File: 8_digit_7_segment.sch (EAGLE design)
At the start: 9 parts, among them IC1 MAX7219CNG

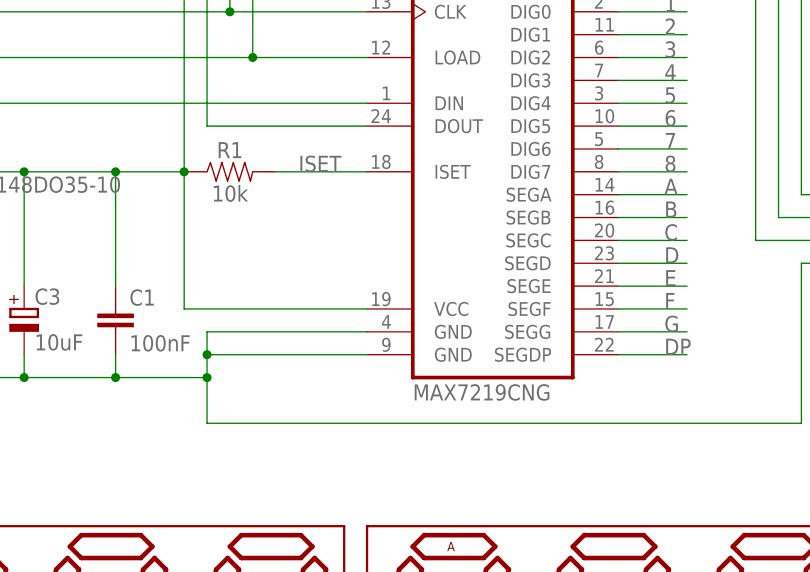
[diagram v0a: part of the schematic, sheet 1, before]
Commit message: Minor modifications, 3D components added to the Eagle files and new images added of the 3D model
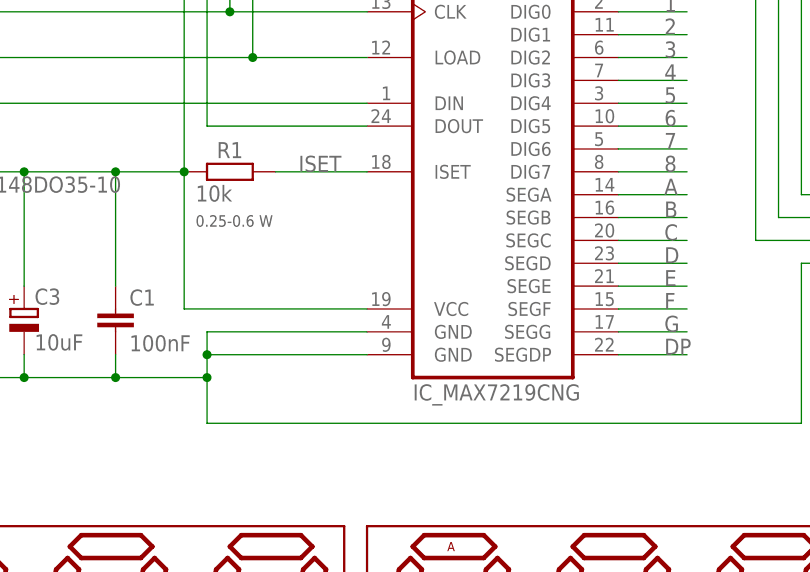
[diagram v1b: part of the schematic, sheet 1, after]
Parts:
- C1: device 001-private-inventory:CAPACITOR_1025-024X044 -> 006-rcl:CAPACITOR_1025-024X044
- C3: device 001-private-inventory:CAPACITOR_POLARIZEDE2-4 -> 006-rcl:CAPACITOR_POLARIZEDE2-5
- D1: device diode:1N4148DO35-10 -> 13-diode:DIODED-10
- IC1: value MAX7219CNG -> IC_MAX7219CNG; device maxim:MAX7219CNG -> 14-displays:IC_MAX7219CNG
- OUTPUT: device SparkFun-Connectors:CONN_05 -> 007-connectors:CONN_051X05/90_FEMALE
- R1: device SparkFun-Resistors:10KOHM-HORIZ-1/6W-5% -> 006-rcl:RESISTOR0207/7
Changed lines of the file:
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@@
 <layer number="18" name="Vias" color="2" fill="1" visible="no" active="no"/>
 <layer number="19" name="Unrouted" color="6" fill="1" visible="no" active="no"/>
-<layer number="20" name="Dimension" color="15" fill="1" visible="no" active="no"/>
-<layer number="21" name="tPlace" color="16" fill="1" visible="no" active="no"/>
+<layer number="20" name="Dimension" color="24" fill="1" visible="no" active="no"/>
+<layer number="21" name="tPlace" color="7" fill="1" visible="no" active="no"/>
 <layer number="22" name="bPlace" color="7" fill="1" visible="no" active="no"/>
 <layer number="23" name="tOrigins" color="15" fill="1" visible="no" active="no"/>
@@
 <layer number="49" name="Reference" color="7" fill="1" visible="no" active="no"/>
 <layer number="50" name="dxf" color="7" fill="1" visible="no" active="no"/>
-<layer number="51" name="tDocu" color="14" fill="1" visible="no" active="no"/>
+<layer number="51" name="tDocu" color="7" fill="1" visible="no" active="no"/>
 <layer number="52" name="bDocu" color="7" fill="1" visible="no" active="no"/>
 <layer number="53" name="tGND_GNDA" color="7" fill="9" visible="no" active="no"/>
@@
 </classes>
 <parts>
-<part name="IC1" library="maxim" library_urn="urn:adsk.eagle:library:269" deviceset="MAX7219CNG" device="" package3d_urn="urn:adsk.eagle:package:17515/1"/>
-<part name="D1" library="diode" library_urn="urn:adsk.eagle:library:210" deviceset="1N4148" device="DO35-10" package3d_urn="urn:adsk.eagle:package:43344/2" value="1N4148DO35-10"/>
-<part name="R1" library="SparkFun-Resistors" deviceset="10KOHM" device="-HORIZ-1/6W-5%" value="10k"/>
-<part name="C3" library="001-private-inventory" deviceset="CAPACITOR_POLARIZED" device="E2-4" package3d_urn="urn:adsk.eagle:package:23347/1" value="10uF"/>
+<part name="IC1" library="14-displays" library_urn="urn:adsk.eagle:library:5805075" deviceset="IC_MAX7219CNG" device="" package3d_urn="urn:adsk.eagle:package:5815011/2"/>
+<part name="D1" library="13-diode" library_urn="urn:adsk.eagle:library:5755551" deviceset="DIODE" device="D-10" package3d_urn="urn:adsk.eagle:package:5797916/3" value="1N4148DO35-10"/>
+<part name="R1" library="006-rcl" library_urn="urn:adsk.eagle:library:5746079" deviceset="RESISTOR" device="0207/7" package3d_urn="urn:adsk.eagle:package:5794443/2" value="10k"/>
+<part name="C3" library="006-rcl" library_urn="urn:adsk.eagle:library:5746079" deviceset="CAPACITOR_POLARIZED" device="E2-5" package3d_urn="urn:adsk.eagle:package:5815177/1" value="10uF"/>
 <part name="INPUT" library="001-private-inventory" deviceset="CONN_05" device="1X05LA" package3d_urn="urn:adsk.eagle:package:22467/2"/>
-<part name="OUTPUT" library="SparkFun-Connectors" deviceset="CONN_05" device=""/>
-<part name="C1" library="001-private-inventory" deviceset="CAPACITOR_1" device="025-024X044" package3d_urn="urn:adsk.eagle:package:23630/1" value="100nF"/>
+<part name="OUTPUT" library="007-connectors" library_urn="urn:adsk.eagle:library:5754142" deviceset="CONN_05" device="1X05/90_FEMALE" package3d_urn="urn:adsk.eagle:package:5793120/2"/>
+<part name="C1" library="006-rcl" library_urn="urn:adsk.eagle:library:5746079" deviceset="CAPACITOR_1" device="025-024X044" package3d_urn="urn:adsk.eagle:package:5815137/3" value="100nF"/>
 <part name="DISP5" library="001-private-inventory" library_urn="urn:adsk.eagle:library:5745527" deviceset="DISPLAY_7_SEGMENT_4DIGIT_20MM" device="-RED" package3d_urn="urn:adsk.eagle:package:5745809/2" value="ATA8041ARBJ "/>
 <part name="DISP6" library="001-private-inventory" library_urn="urn:adsk.eagle:library:5745527" deviceset="DISPLAY_7_SEGMENT_4DIGIT_20MM" device="-RED" package3d_urn="urn:adsk.eagle:package:5745809/2" value="ATA8041ARBJ "/>
@@
 <instance part="R1" gate="G$1" x="-22.86" y="73.66">
 <attribute name="NAME" x="-22.86" y="75.184" size="1.778" layer="95" font="vector" align="bottom-center"/>
-<attribute name="VALUE" x="-22.86" y="72.136" size="1.778" layer="96" font="vector" align="top-center"/>
 </instance>
 <instance part="C3" gate="G$1" x="-45.72" y="58.42">
